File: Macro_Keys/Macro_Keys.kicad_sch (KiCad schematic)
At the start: 42 parts, among them J1 ICSP, J2 OLED, J3 USB_C_Receptacle_USB2.0, SW1 RST, SW10 SW, SW11 Mode, SW2 SW, SW3 SW, SW4 SW, SW5 SW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

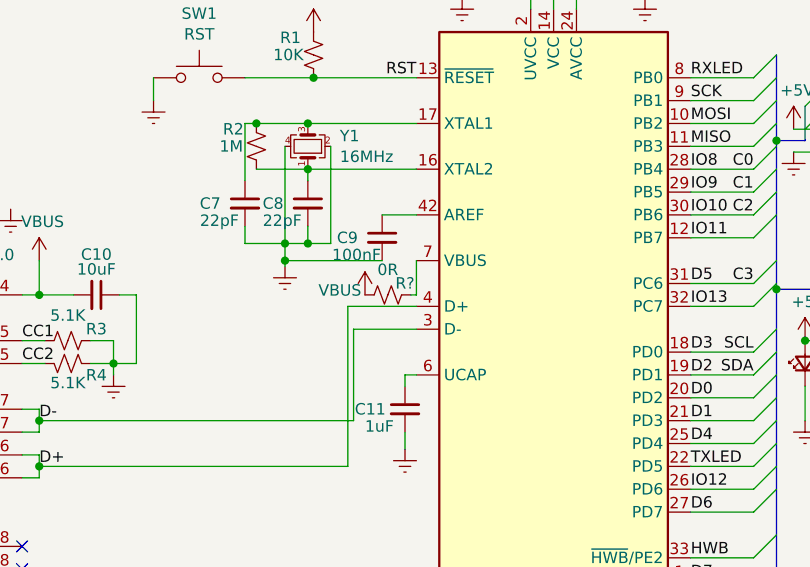
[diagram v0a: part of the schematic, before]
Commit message: Macro_Keys Layout complete + Programmer WIP
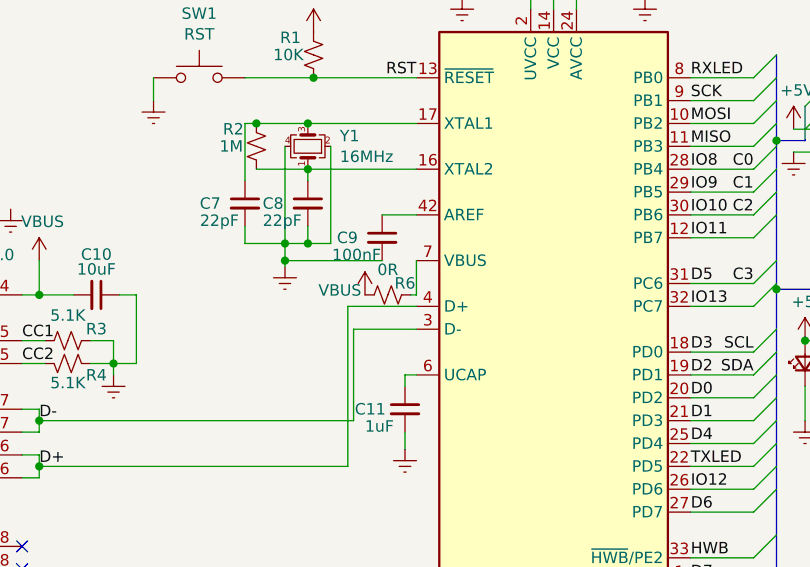
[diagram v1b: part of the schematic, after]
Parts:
- gave numbers to parts that had none: 1
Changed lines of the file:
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@@
   (symbol (lib_name "Device:R_Small_US_2") (lib_id "Device:R_Small_US") (at 85.725 83.82 90) (unit 1)
     (in_bom yes) (on_board yes)
-    (property "Reference" "R?" (id 0) (at 87.63 82.5308 90))
+    (property "Reference" "R6" (id 0) (at 87.63 82.5308 90))
     (property "Value" "0R" (id 1) (at 85.725 81.0195 90))
     (property "Footprint" "Resistor_SMD:R_0805_2012Metric" (id 2) (at 85.725 83.82 0)
@@
     )
     (path "/0ed5f2e9-5127-4c20-9111-bfb6c6221fcd"
-      (reference "R?") (unit 1)
+      (reference "R6") (unit 1)
     )
     (path "/510647f7-4df5-4bc8-8466-492f70d9d5b4"
